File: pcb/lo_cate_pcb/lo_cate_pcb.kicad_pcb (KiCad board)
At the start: 2 copper layers, 100 x 100 mm, 45 parts, among them J1 Conn_01x07_Pin, J2 690-005-299-043, SW1 MICRO_RESET, SW2 MICRO_ON, SW3 BUTTON1, SW4 BUTTON2, SW5 BUTTON3, U1 STM32F401RETx, U2 BMI323, U3 LED1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

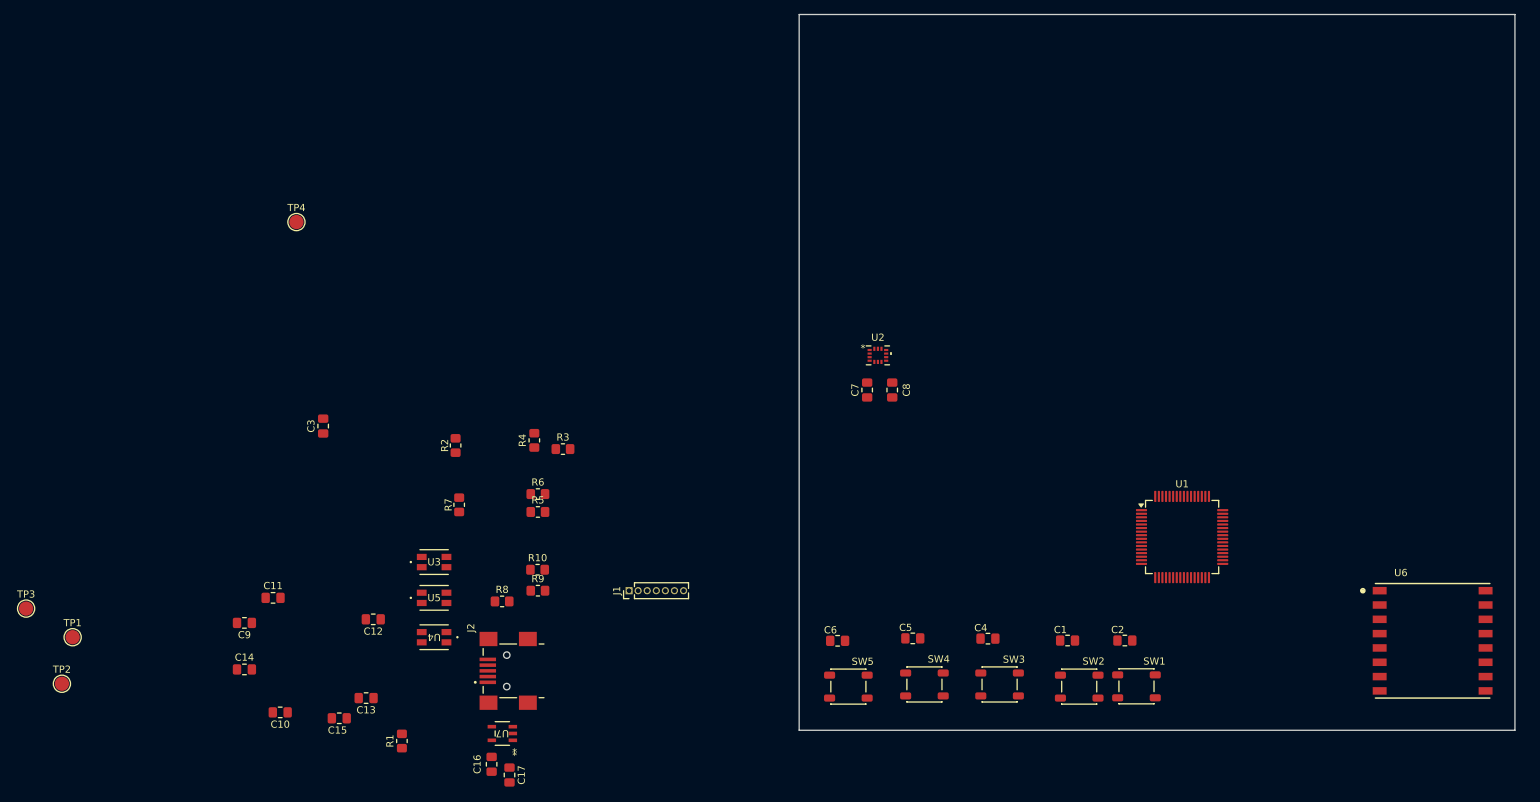
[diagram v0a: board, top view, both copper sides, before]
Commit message: Added smt connector
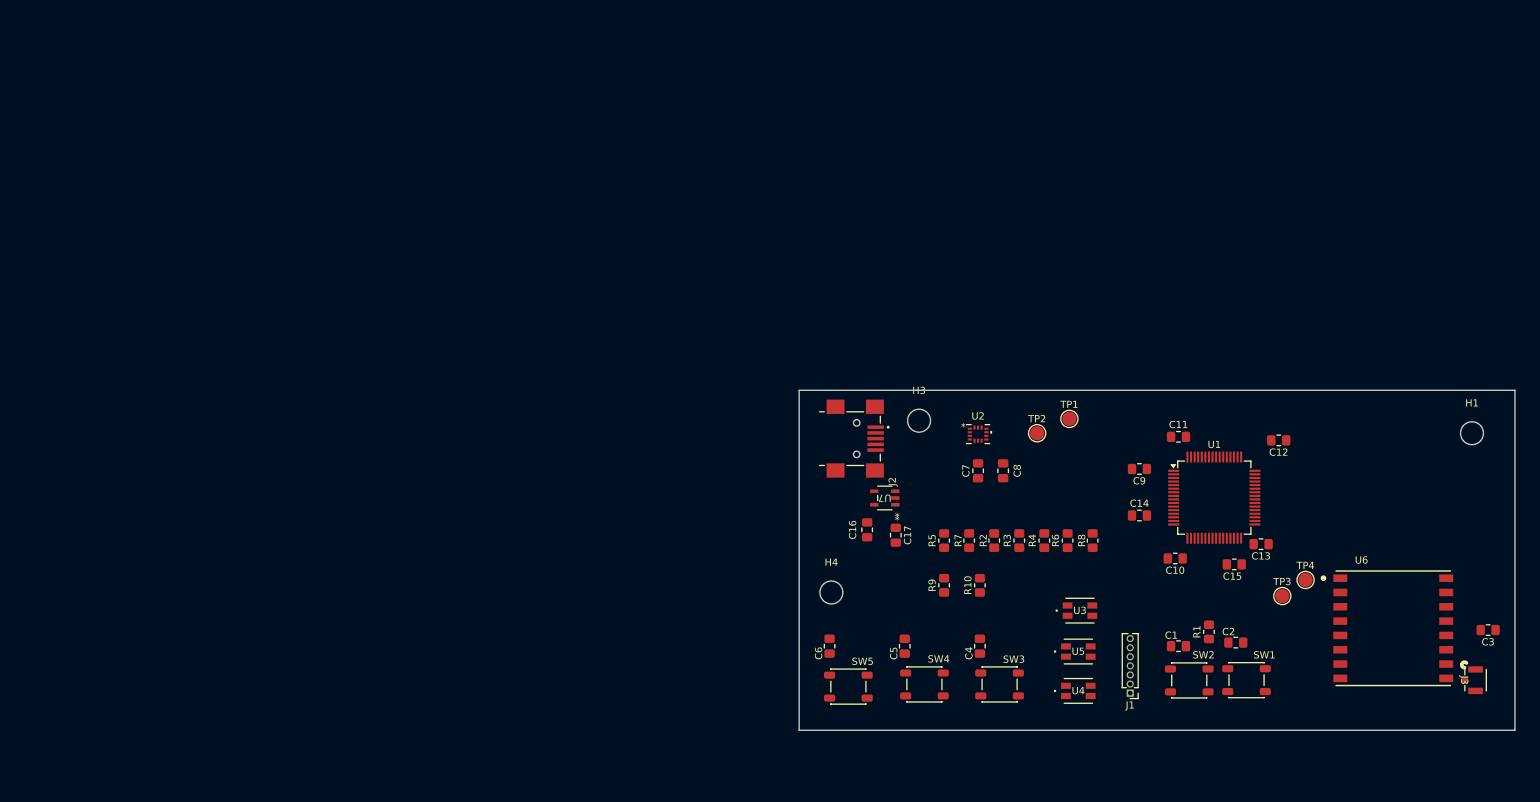
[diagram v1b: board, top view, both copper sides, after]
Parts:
- added H1: MountingHole, MountingHole:MountingHole_3.2mm_M3, F.Cu at (252.5, 103.5)
- added H3: MountingHole, MountingHole:MountingHole_3.2mm_M3, F.Cu at (175.2, 101.8)
- added H4: MountingHole, MountingHole:MountingHole_3.2mm_M3, F.Cu at (163.0, 125.8)
- added J3: U.FL-R-SMT-110, footprints:CONN1_UFL-R_HIR, F.Cu at (253.0, 138.0)
- moved TP3 175.5 mm to (226.0, 126.2)
- moved C3 165.2 mm to (254.8, 131.0), turned to 180 degrees
- moved TP4 149.6 mm to (229.2, 124.0)
- moved TP1 142.6 mm to (196.2, 101.5)
- moved TP2 140.7 mm to (191.8, 103.5)
- moved C12 128.9 mm to (225.5, 104.5)
- moved C11 128.5 mm to (211.5, 104.0)
- moved C10 126.9 mm to (211.0, 121.0)
- moved C13 126.9 mm to (223.0, 119.0)
- moved C14 126.9 mm to (206.0, 115.0)
- moved C15 126.9 mm to (219.3, 121.8)
- moved C9 126.9 mm to (206.0, 108.5)
- moved R1 113.8 mm to (215.8, 131.2)
- moved U3 90.5 mm to (197.7, 128.3)
- moved U4 90.3 mm to (197.5, 139.5), turned to 0 degrees
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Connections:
- U6 pad 9: /LORA_ANTENNA -> Net-(U6-ANT)
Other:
- board size 100 x 100 mm -> 100 x 47.5 mm

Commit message: Most PCB Routing is complete
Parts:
- moved H3 68.6 mm to (230.0, 143.0)
- moved R2 53.9 mm to (239.3, 113.3), turned to 90 degrees
- moved R3 53.9 mm to (242.8, 113.3), turned to -90 degrees
- moved U4 53.5 mm to (241.3, 108.8)
- moved R4 52.5 mm to (243.3, 104.6)
- moved C12 37.2 mm to (194.5, 125.0), turned to 0 degrees
- moved R8 31.8 mm to (168.2, 124.4), turned to 90 degrees
- moved U5 30.7 mm to (170.2, 119.9)
- moved U3 28.1 mm to (169.9, 132.4)
- moved C13 27.9 mm to (196.2, 111.4), turned to -90 degrees
- moved R6 25.3 mm to (172.9, 128.9), turned to 0 degrees
- moved C11 25.2 mm to (206.6, 128.7), turned to 90 degrees
- moved R7 23.3 mm to (167.9, 136.9), turned to 90 degrees
- moved C15 23.2 mm to (199.6, 109.5), turned to 90 degrees
- moved R5 18.7 mm to (172.5, 136.1), turned to 0 degrees
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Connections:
- C16 pad 1: /3v3 -> /3V3
- U7 pad 5: /3v3 -> /3V3
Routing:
- net /3V3: track 0.00 -> 96.5 mm, vias 0 -> 18
- net /MICRO_WAKEUP: track 0.00 -> 66.5 mm
- net /LED2_RED: track 0.00 -> 50.0 mm, vias 0 -> 2
- net /LED1_BLUE: track 0.00 -> 46.5 mm, vias 0 -> 2
- net /NRST: track 0.00 -> 45.2 mm, vias 0 -> 2
- net /USB_DM: track 0.00 -> 43.0 mm, vias 0 -> 2
- net /BUTTON3: track 0.00 -> 42.3 mm, vias 0 -> 2
- net /LORA_RST: track 0.00 -> 42.1 mm, vias 0 -> 2
- net /LORA_CSB: track 0.00 -> 41.8 mm, vias 0 -> 2
- net /USB_DP: track 0.00 -> 41.5 mm, vias 0 -> 2
- net /LORA_SCK: track 0.00 -> 41.2 mm, vias 0 -> 2
- net /LED2_GREEN: track 0.00 -> 39.7 mm
- net /BUTTON1: track 0.00 -> 39.4 mm, vias 0 -> 2
- net /BUTTON2: track 0.00 -> 37.8 mm, vias 0 -> 2
- net /USB_ID: track 0.00 -> 37.8 mm
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- added copper zone on B.Cu, net /3V3
- added copper zone on F.Cu, net GND
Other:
- board size 100 x 47.5 mm -> 100 x 50 mm

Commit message: Final PCB design done
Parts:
- removed J3: U.FL-R-SMT-110, footprints:CONN1_UFL-R_HIR
- added G***: LOGO, footprints:Logo_CADPAD_2, F.Cu at (217.2, 105.8)
- added H4: MountingHole, MountingHole:MountingHole_3.2mm_M3, F.Cu at (161.8, 117.4)
- added U8: 734120114, footprints:73412-0114_MOL, F.Cu at (249.0, 142.0)
- renumbered TP1 to MISO, TP3 to MISO, TP2 to MOSI, TP4 to MOSI
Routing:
- net GND: track 20.2 -> 28.6 mm
- net Net-(U6-ANT): track 0.00 -> 2.84 mm
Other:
- board text added: "3V3"
- board text added: "BOOTO"
- board text added: "BUTTON 1"
- board text added: "BUTTON 2"
- board text added: "BUTTON 3"
- board text added: "GND"
- board text added: "LED1"
- board text added: "LED3"
- board text added: "MCU RST"
- board text added: "MCU WKUP"
- board text added: "NRST"
- board text added: "SWCLK"
- board text added: "SWDIO"
- board text added: "SWO"

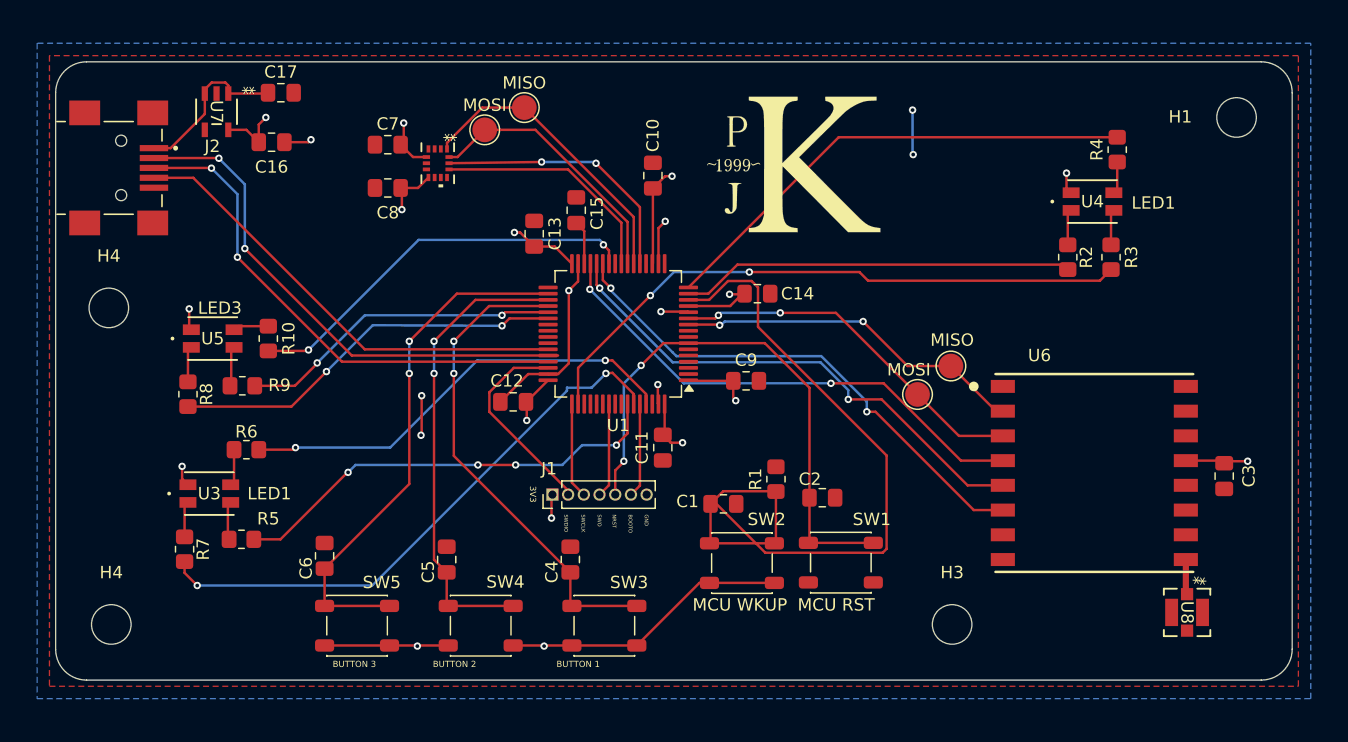
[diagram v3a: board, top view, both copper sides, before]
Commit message: Changed PCB to a 4 Layer Version
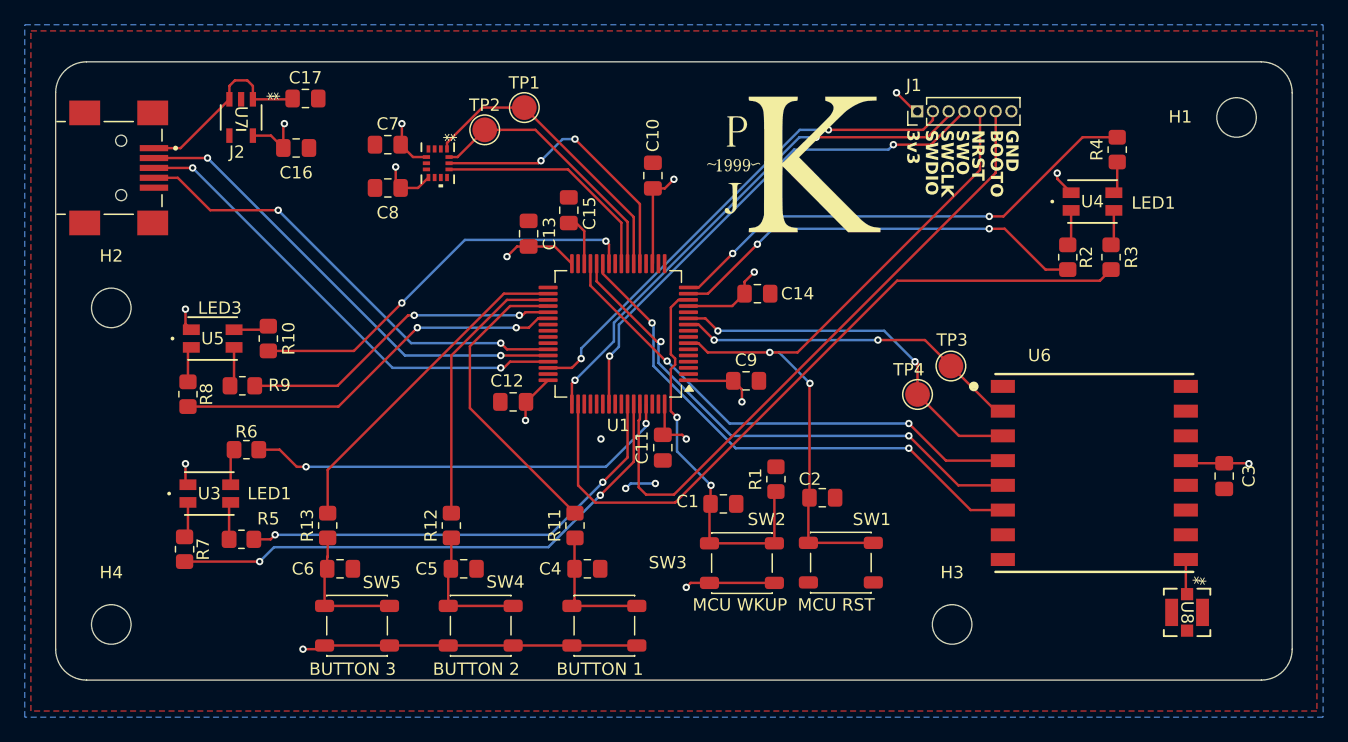
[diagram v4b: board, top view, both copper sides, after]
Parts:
- removed the H4 at (161.8, 117.4)
- added H2: MountingHole, MountingHole:MountingHole_3.2mm_M3, F.Cu at (162.0, 117.4)
- added R11: 50k, Resistor_SMD:R_0805_2012Metric_Pad1.20x1.40mm_HandSolder, F.Cu at (199.5, 135.0)
- added R12: 50k, Resistor_SMD:R_0805_2012Metric_Pad1.20x1.40mm_HandSolder, F.Cu at (189.5, 135.0)
- added R13: 50k, Resistor_SMD:R_0805_2012Metric_Pad1.20x1.40mm_HandSolder, F.Cu at (179.5, 135.0)
- moved J1 42.8 mm to (227.2, 101.5)
- moved U7 2.04 mm to (172.5, 102.0)
- moved C16 2.04 mm to (177.0, 104.5)
- moved C17 2.04 mm to (177.7, 100.5)
- moved C6 1.63 mm to (180.5, 138.5), turned to 180 degrees
- moved C4 1.57 mm to (200.5, 138.5), turned to 180 degrees
- moved C5 1.57 mm to (190.5, 138.5), turned to 180 degrees
- moved C15 0.60 mm to (199.0, 109.5)
- moved C13 0.45 mm to (195.8, 111.4)
- renumbered MISO to TP1, MOSI to TP2, MISO to TP3, MOSI to TP4
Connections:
- C4 pad 2: /BUTTON1 -> Net-(C4-Pad2)
- C5 pad 2: /BUTTON2 -> Net-(C5-Pad2)
- C6 pad 2: /BUTTON3 -> Net-(C6-Pad2)
- SW3 pad 2: /BUTTON1 -> Net-(C4-Pad2)
- SW4 pad 2: /BUTTON2 -> Net-(C5-Pad2)
- SW5 pad 2: /BUTTON3 -> Net-(C6-Pad2)
- U2 pad 4: /IMU_INT1 -> unconnected-(U2-INT1-Pad4)
- U2 pad 9: /IMU_INT2 -> unconnected-(U2-INT2-Pad9)
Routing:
- net /BOOTO: track 7.63 -> 51.6 mm
- net /SWCLK: track 7.72 -> 42.4 mm, vias 0 -> 2
- net /MICRO_WAKEUP: track 66.5 -> 31.9 mm, vias 0 -> 2
- net /SWO: track 7.64 -> 41.8 mm, vias 0 -> 2
- net GND: track 28.6 -> 2.57 mm, vias 7 -> 3
- net /SWDIO: track 16.5 -> 40.6 mm, vias 0 -> 2
- net /BUTTON2: track 37.8 -> 22.4 mm, vias 2 -> 0
- net /BUTTON3: track 42.3 -> 27.2 mm, vias 2 -> 0
- net /BUTTON1: track 39.4 -> 24.7 mm, vias 2 -> 0
- net /NRST: track 45.2 -> 57.2 mm
- net Net-(C5-Pad2): track 0.00 -> 11.4 mm
- net Net-(C6-Pad2): track 0.00 -> 10.9 mm
- net Net-(C4-Pad2): track 0.00 -> 10.9 mm
- net /LED2_RED: track 50.0 -> 58.1 mm, vias 2 -> 0
- net /USB_DM: track 43.0 -> 38.5 mm
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- added copper zone on In2.Cu, net /3V3
- added copper zone on B.Cu, net GND
- added copper zone on In1.Cu, net GND
- removed copper zone on B.Cu, net /3V3
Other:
- copper layers 2 -> 4
- board text added: "3v3"
- board text removed: "3V3"

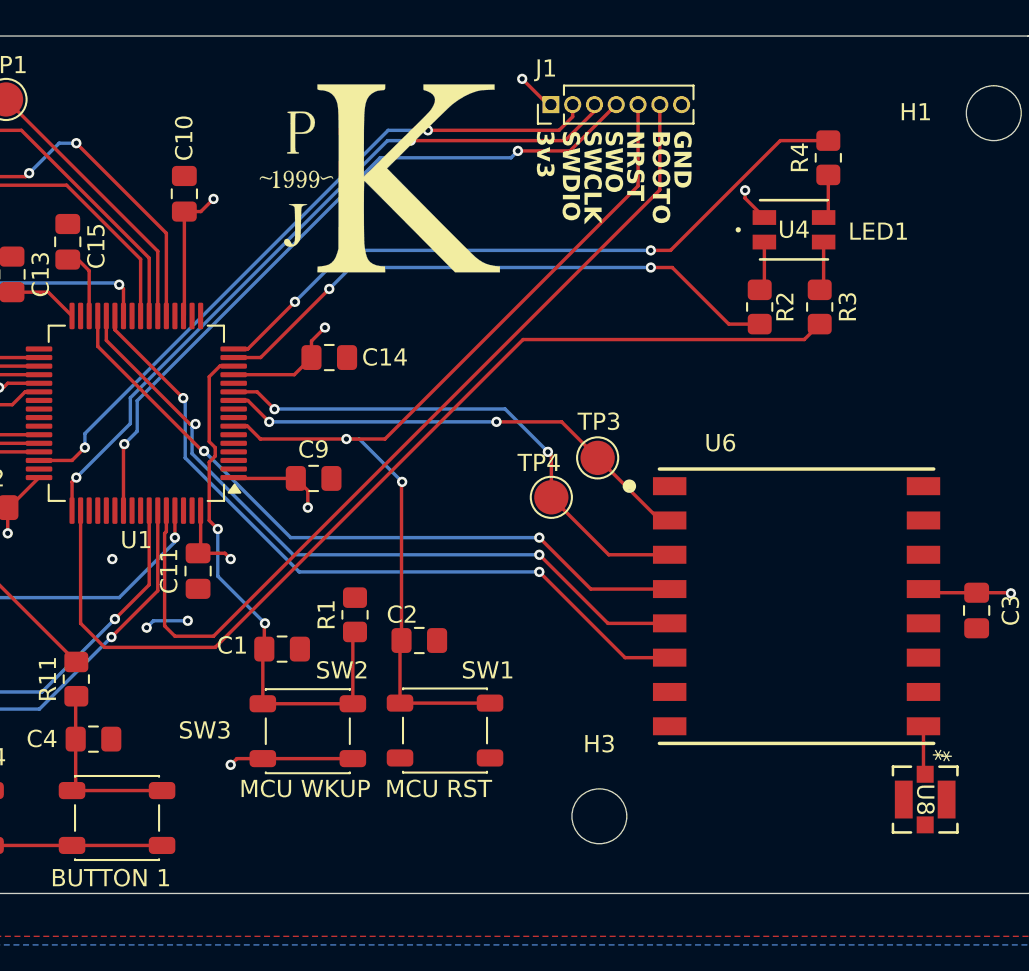
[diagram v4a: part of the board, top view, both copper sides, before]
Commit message: Added an external crystal oscillator
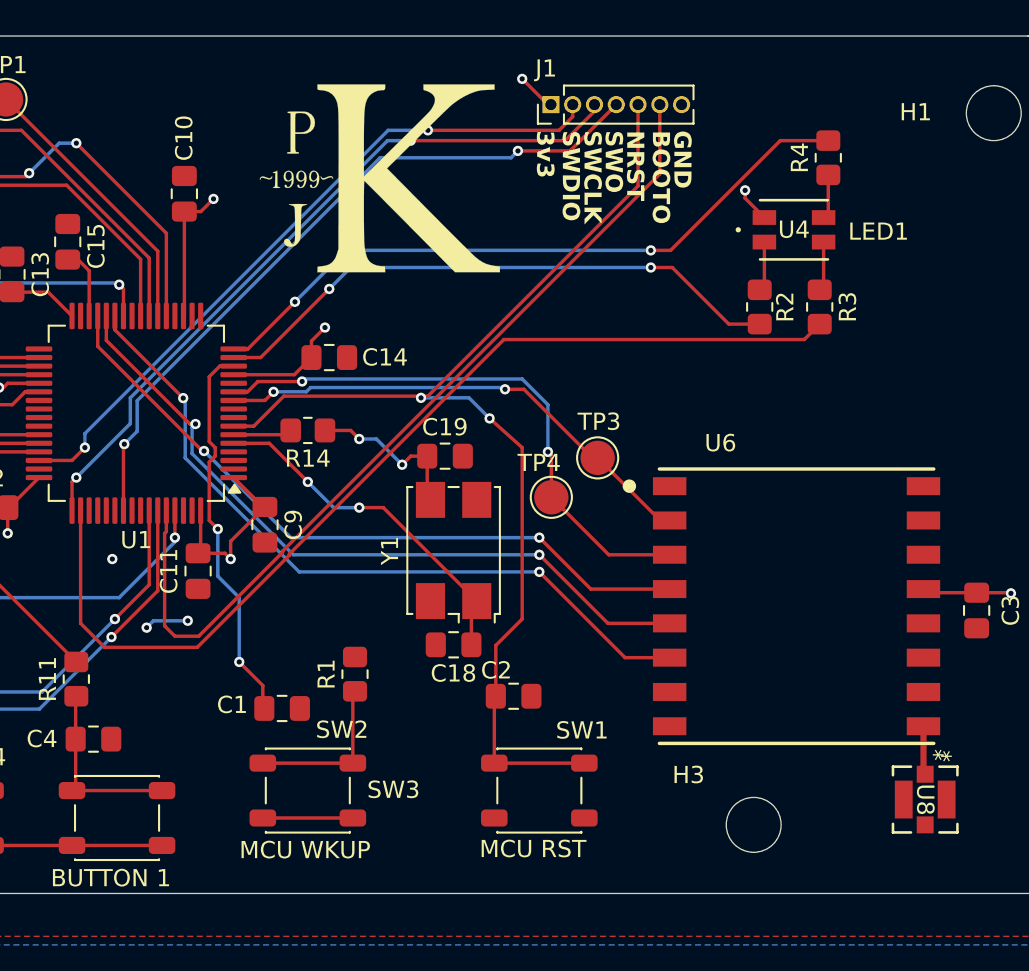
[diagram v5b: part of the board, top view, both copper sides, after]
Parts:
- added C18: 10p, Capacitor_SMD:C_0805_2012Metric_Pad1.18x1.45mm_HandSolder, F.Cu at (221.5, 133.0)
- added C19: 10p, Capacitor_SMD:C_0805_2012Metric_Pad1.18x1.45mm_HandSolder, F.Cu at (221.0, 122.0)
- added R14: 30R, Resistor_SMD:R_0805_2012Metric_Pad1.20x1.40mm_HandSolder, F.Cu at (213.0, 120.5)
- added Y1: Crystal_GND24_Small, Crystal:Crystal_SMD_7050-4Pin_7.0x5.0mm, F.Cu at (221.5, 127.5)
- moved H3 9.01 mm to (239.0, 143.5)
- moved SW1 6.52 mm to (226.5, 141.5)
- moved C2 6.39 mm to (225.0, 136.0)
- moved C9 3.92 mm to (210.5, 126.0), turned to -90 degrees
- moved C1 3.46 mm to (211.5, 136.7)
- moved R1 3.46 mm to (215.8, 134.7)
- moved SW2 3.46 mm to (213.0, 141.5)
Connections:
- U1 pad 5: unconnected-(U1-PH0-Pad5) -> /OSC_IN
- U1 pad 6: unconnected-(U1-PH1-Pad6) -> /OSC_OUT
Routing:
- net /OSC_IN: track 0.00 -> 20.7 mm, vias 0 -> 2
- net Net-(C19-Pad1): track 0.00 -> 9.63 mm, vias 0 -> 2
- net /NRST: track 57.2 -> 65.5 mm
- net /OSC_OUT: track 0.00 -> 3.43 mm
- net /LORA_MOSI: track 30.8 -> 33.0 mm
- net /3V3: track 96.4 -> 95.1 mm, vias 16 -> 14
- net /LORA_MISO: track 28.3 -> 28.9 mm
- net /BOOTO: track 51.6 -> 51.1 mm

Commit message: Finished PCB?
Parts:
- moved G*** 2.20 mm to (215.0, 105.9)
- moved C14 1.84 mm to (215.2, 114.7)
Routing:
- net /MICRO_WAKEUP: track 31.8 -> 35.6 mm
- net /3V3: track 95.1 -> 97.8 mm, vias 14 -> 15
